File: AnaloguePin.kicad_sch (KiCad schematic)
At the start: 9 parts, among them J5 ADC

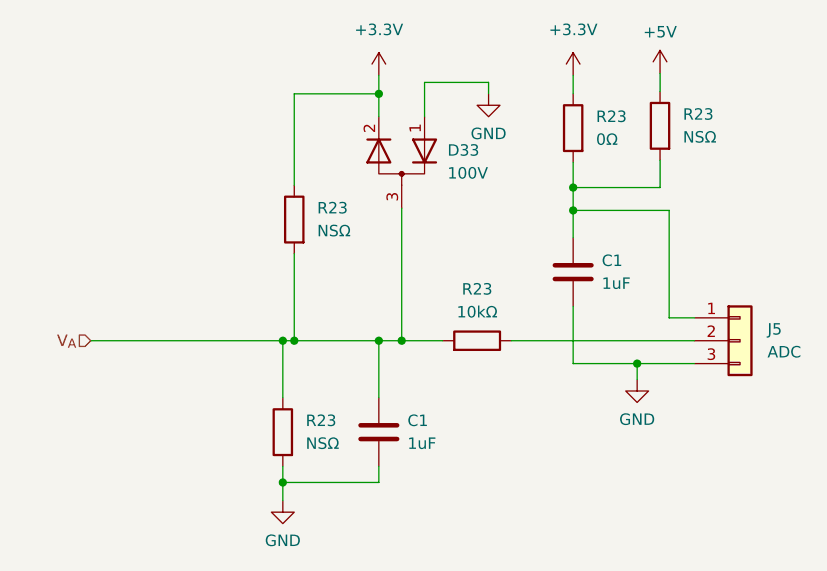
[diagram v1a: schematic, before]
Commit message: Finished schematic. Move to PCB.
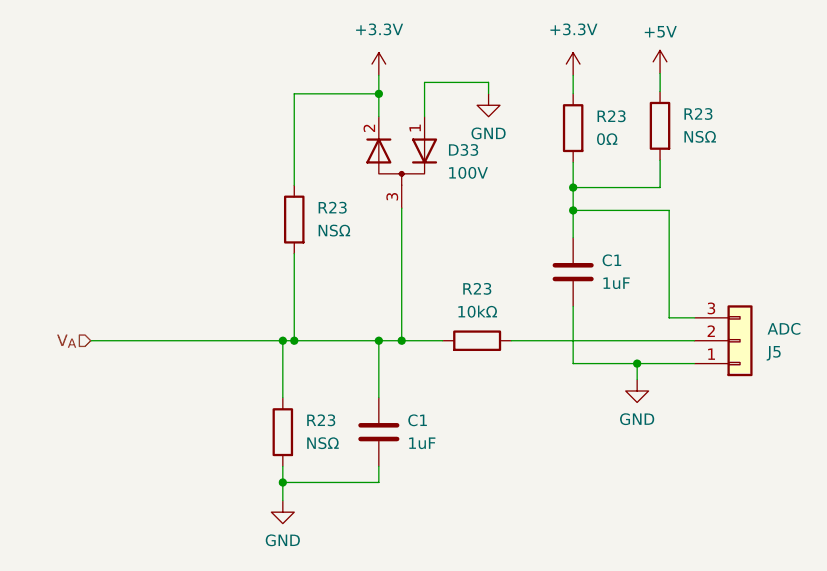
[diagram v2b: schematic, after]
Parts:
- J5: footprint (none) -> Connector_PinHeader_2.54mm:PinHeader_1x03_P2.54mm_Vertical
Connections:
- net GND: now also J5.1 (Pin_1); no longer J5.3 (Pin_3)
- net at C1.1, R23.2, R23.2: now also J5.3 (Pin_3); no longer J5.1 (Pin_1)
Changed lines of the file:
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@@
   (symbol (lib_id "power:GND") (at 136.652 97.028 0) (unit 1)
     (in_bom yes) (on_board yes) (dnp no) (fields_autoplaced)
-    (property "Reference" "#PWR046" (at 136.652 103.378 0)
+    (property "Reference" "#PWR01" (at 136.652 103.378 0)
       (effects (font (size 1.27 1.27)) hide)
     )
@@
   (symbol (lib_id "power:GND") (at 159.512 51.816 0) (unit 1)
     (in_bom yes) (on_board yes) (dnp no) (fields_autoplaced)
-    (property "Reference" "#PWR043" (at 159.512 58.166 0)
+    (property "Reference" "#PWR06" (at 159.512 58.166 0)
       (effects (font (size 1.27 1.27)) hide)
     )
@@
   (symbol (lib_id "power:GND") (at 176.022 83.566 0) (unit 1)
     (in_bom yes) (on_board yes) (dnp no) (fields_autoplaced)
-    (property "Reference" "#PWR043" (at 176.022 89.916 0)
+    (property "Reference" "#PWR04" (at 176.022 89.916 0)
       (effects (font (size 1.27 1.27)) hide)
     )
@@
     )
   )
-  (symbol (lib_id "Connector_Generic:Conn_01x03") (at 187.452 79.248 0) (unit 1)
-    (in_bom yes) (on_board yes) (dnp no) (fields_autoplaced)
-    (property "Reference" "J5" (at 190.5 77.978 0)
+  (symbol (lib_id "Connector_Generic:Conn_01x03") (at 187.452 79.248 0) (mirror x) (unit 1)
+    (in_bom yes) (on_board yes) (dnp no)
+    (property "Reference" "J5" (at 190.5 80.518 0)
       (effects (font (size 1.27 1.27)) (justify left))
     )
-    (property "Value" "ADC" (at 190.5 80.518 0)
+    (property "Value" "ADC" (at 190.5 77.978 0)
       (effects (font (size 1.27 1.27)) (justify left))
     )
-    (property "Footprint" "" (at 187.452 79.248 0)
-      (effects (font (size 1.27 1.27)) hide)
-    )
+    (property "Footprint" "Connector_PinHeader_2.54mm:PinHeader_1x03_P2.54mm_Vertical" (at 187.452 79.248 0)
+      (effects (font (size 1.27 1.27)) hide)
+    )
